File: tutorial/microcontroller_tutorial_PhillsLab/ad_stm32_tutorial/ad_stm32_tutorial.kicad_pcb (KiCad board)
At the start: 2 copper layers, 0 parts

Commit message: Started PCB Layout of power section
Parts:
- added C1: 4u7, Capacitor_SMD:C_0805_2012Metric, F.Cu at (91.8, 104.5)
- added C10: 100n, Capacitor_SMD:C_0603_1608Metric, F.Cu at (69.5, 95.4)
- added C11: 10p, Capacitor_SMD:C_0603_1608Metric, F.Cu at (69.5, 97.9)
- added C12: 10p, Capacitor_SMD:C_0603_1608Metric, F.Cu at (69.5, 100.4)
- added C13: 100n, Capacitor_SMD:C_0603_1608Metric, F.Cu at (69.5, 102.9)
- added C14: 100n, Capacitor_SMD:C_0603_1608Metric, F.Cu at (69.5, 105.4)
- added C2: 4u7, Capacitor_SMD:C_0805_2012Metric, F.Cu at (91.8, 107.5)
- added C3: 22p, Capacitor_SMD:C_0603_1608Metric, F.Cu at (65.5, 92.9)
- added C4: 100n, Capacitor_SMD:C_0603_1608Metric, F.Cu at (129.5, 95.0)
- added C5: 100n, Capacitor_SMD:C_0603_1608Metric, F.Cu at (131.5, 95.0)
- added C6: 100n, Capacitor_SMD:C_0603_1608Metric, F.Cu at (65.5, 100.4)
- added C7: 100n, Capacitor_SMD:C_0603_1608Metric, F.Cu at (65.5, 102.9)
- added C8: 100n, Capacitor_SMD:C_0603_1608Metric, F.Cu at (65.5, 105.4)
- added C9: 100n, Capacitor_SMD:C_0603_1608Metric, F.Cu at (69.5, 92.9)
- added FB1: 120R, Inductor_SMD:L_0603_1608Metric, F.Cu at (130.5, 92.5)
- added FB2: 120R, Inductor_SMD:L_6.3x6.3_H3, F.Cu at (79.8, 103.4)
- added J1: USB_C_Receptacle_USB2.0_16P, Connector_USB:USB_C_Receptacle_GCT_USB4105-xx-A_16P_TopMnt_Horizontal, F.Cu at (123.0, 91.5)
- added J2: TagConnect_TC2030-NL, Connector:Tag-Connect_TC2030-IDC-NL_2x03_P1.27mm_Vertical, F.Cu at (88.1, 94.2)
- added J3: Conn_01x06, Connector_JST:JST_EH_S6B-EH_1x06_P2.50mm_Horizontal, F.Cu at (67.2, 85.5)
- added L1: NRH2412T100MNGH, Inductor_SMD:NRH2412T2R2MNGH, F.Cu at (86.8, 105.7)
- added R1: 887k, Resistor_SMD:R_0603_1608Metric, F.Cu at (73.5, 92.9)
- added R2: 887k, Resistor_SMD:R_0603_1608Metric, F.Cu at (73.5, 95.4)
- added R3: 5k1, Resistor_SMD:R_0603_1608Metric, F.Cu at (126.2, 85.2)
- added R4: 5k1, Resistor_SMD:R_0603_1608Metric, F.Cu at (126.2, 97.8)
- added R5: 5k1, Resistor_SMD:R_0603_1608Metric, F.Cu at (73.5, 102.9)
- added U1: ~, Package_TO_SOT_SMD:SOT-23-6, F.Cu at (72.2, 109.1)
- added U2: STM32F042G6Ux, Package_DFN_QFN:QFN-28_4x4mm_P0.5mm, F.Cu at (87.2, 99.8)
- added U3: ~, Package_LGA:LGA-16_4.5x3mm_P0.5mm, F.Cu at (66.7, 109.1)
- added Y2: Crystal_GND24, Crystal:Crystal_SMD_TXC_7M-4Pin_3.2x2.5mm, F.Cu at (93.0, 98.9)
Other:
- board outline added: 35 x 25 mm

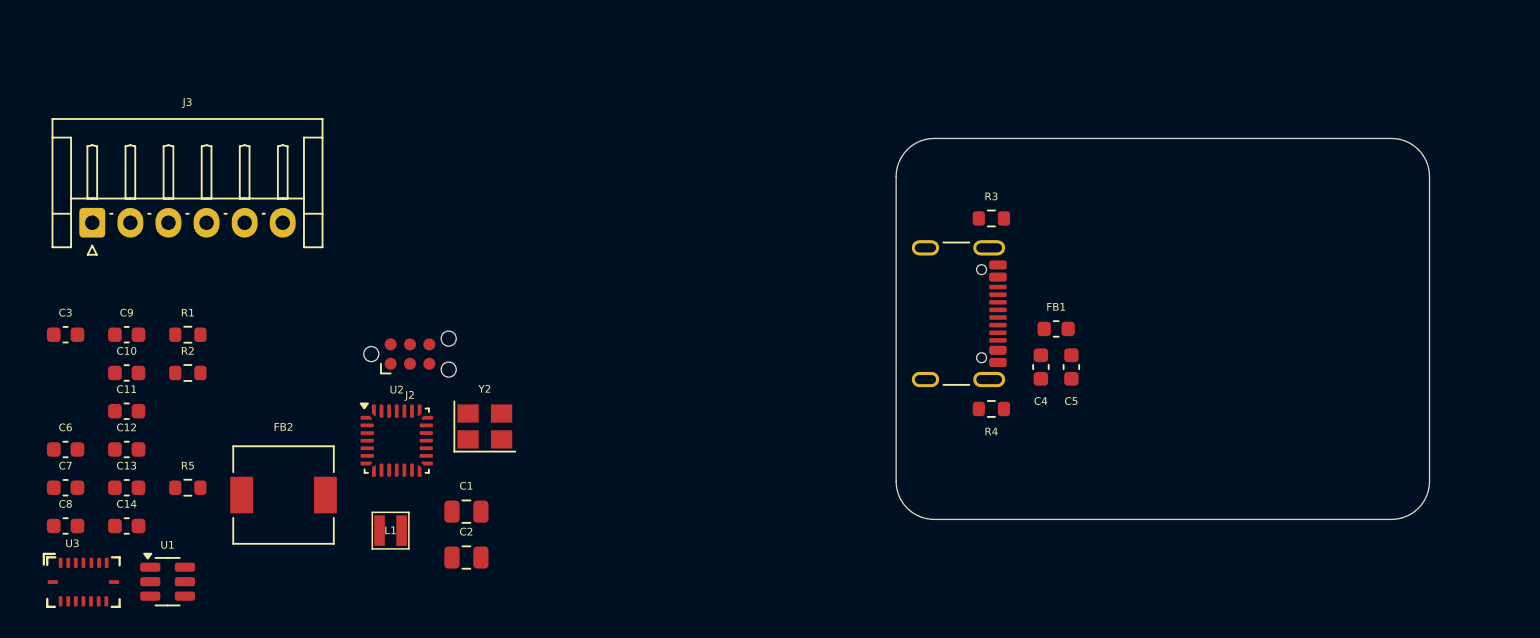
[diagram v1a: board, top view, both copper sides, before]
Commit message: Started adding MCU (STM32F4) and it's components
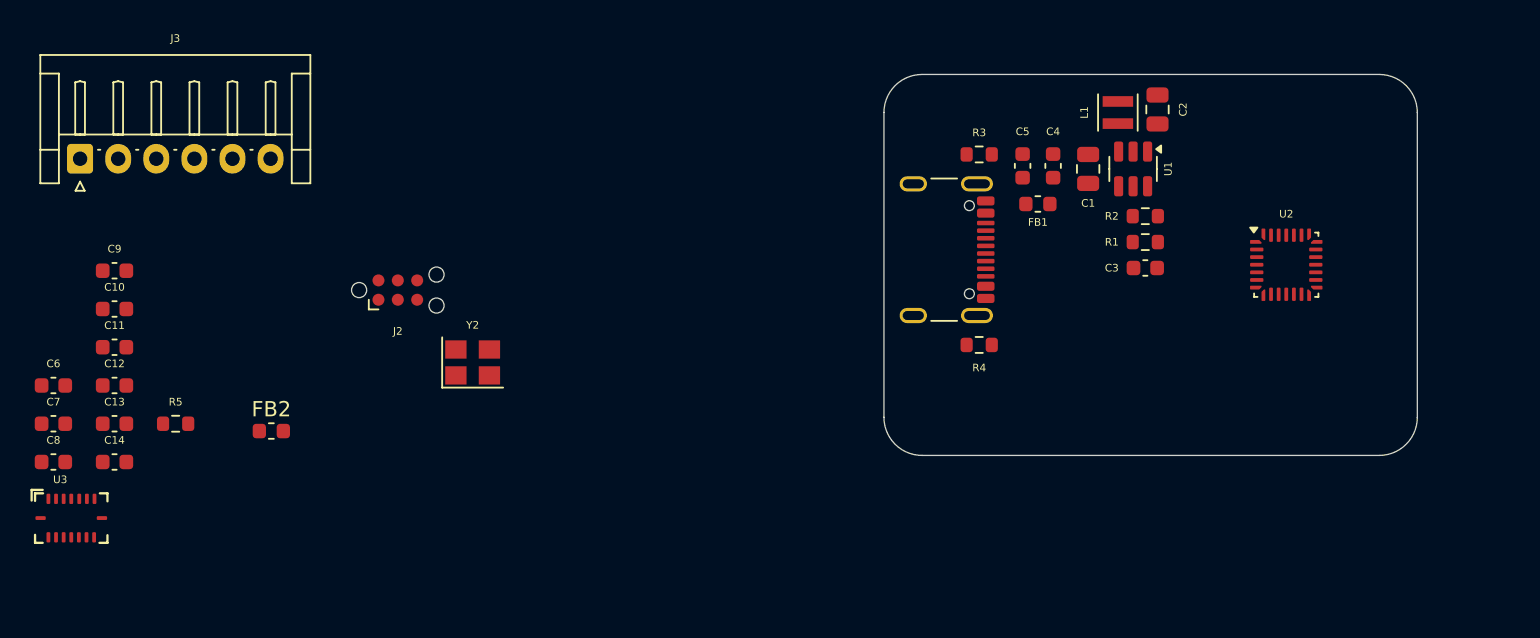
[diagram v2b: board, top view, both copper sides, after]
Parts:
- FB2: footprint Inductor_SMD:L_6.3x6.3_H3 -> Inductor_SMD:L_0603_1608Metric
- L1: footprint Inductor_SMD:NRH2412T2R2MNGH -> Inductor_SMD:L_Taiyo-Yuden_NR-24xx
- moved C3 71.0 mm to (136.3, 88.5)
- moved U1 68.9 mm to (135.6, 82.0), turned to -90 degrees
- moved R2 63.7 mm to (136.3, 85.1)
- moved R1 63.1 mm to (136.3, 86.8)
- moved U2 59.5 mm to (145.6, 88.3)
- moved L1 55.0 mm to (134.6, 78.3), turned to 90 degrees
- moved C2 54.0 mm to (137.2, 78.1), turned to -90 degrees
- moved C1 46.6 mm to (132.6, 82.0), turned to 90 degrees
- moved C5 13.6 mm to (128.3, 81.8), turned to 90 degrees
- moved C4 13.2 mm to (130.3, 81.8), turned to 90 degrees
- moved FB1 8.29 mm to (129.3, 84.3), turned to 180 degrees
- moved C10 4.28 mm to (68.7, 91.2)
- moved C11 4.28 mm to (68.7, 93.7)
- moved C12 4.28 mm to (68.7, 96.2)
- moved C13 4.28 mm to (68.7, 98.7)
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
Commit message: Finished placement of all the components
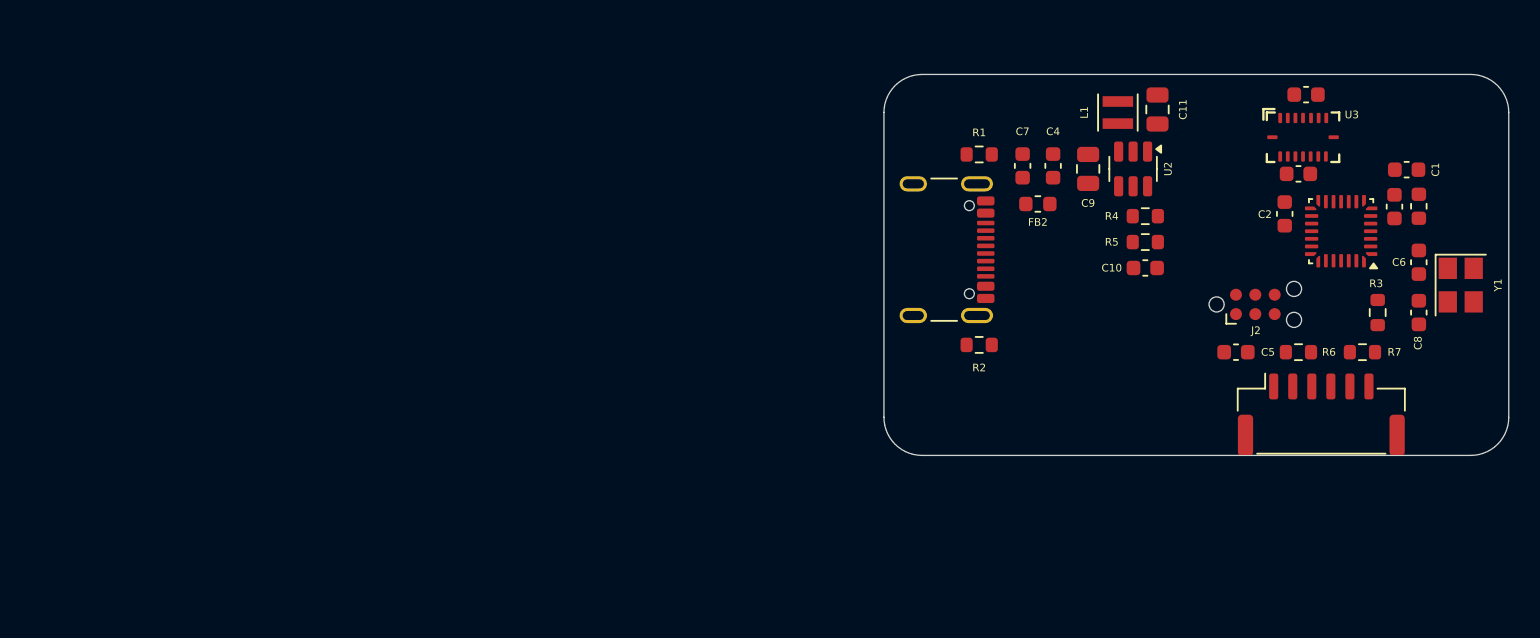
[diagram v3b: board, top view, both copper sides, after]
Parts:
- removed the C7 at (64.7, 98.7)
- added R6: 5k1, Resistor_SMD:R_0603_1608Metric, F.Cu at (146.4, 94.0)
- added R7: 5k1, Resistor_SMD:R_0603_1608Metric, F.Cu at (150.6, 94.0)
- J3: footprint Connector_JST:JST_EH_S6B-EH_1x06_P2.50mm_Horizontal -> Connector_JST:JST_GH_SM06B-GHS-TB_1x06-1MP_P1.25mm_Horizontal
- moved C1 90.8 mm to (153.5, 82.0), turned to 180 degrees
- moved C6 85.8 mm to (154.3, 88.1), turned to -90 degrees
- moved C8 85.7 mm to (154.3, 91.4), turned to 90 degrees
- moved U3 84.6 mm to (146.7, 79.9)
- moved C3 84.1 mm to (152.7, 84.5), turned to 90 degrees
- moved J3 83.2 mm to (147.9, 98.1)
- moved C12 81.8 mm to (146.9, 77.1)
- moved C2 81.6 mm to (145.5, 85.0), turned to -90 degrees
- moved C13 79.4 mm to (146.4, 82.3), turned to 180 degrees
- moved R3 79.2 mm to (151.6, 91.4), turned to -90 degrees
- moved FB1 76.7 mm to (154.3, 84.5), turned to -90 degrees
- moved C5 73.6 mm to (142.3, 94.0)
- moved Y1 65.0 mm to (157.1, 89.6), turned to -90 degrees
- moved J2 56.3 mm to (143.6, 90.9)
- moved U1 4.22 mm to (149.2, 86.1), turned to 180 degrees
- renumbered C8 to C1, C3 to C10, C2 to C11, C14 to C12, C6 to C2, C9 to C3, C10 to C5, C11 to C6, C5 to C7, C12 to C8, C1 to C9, FB2 to FB1, FB1 to FB2, R3 to R1, R4 to R2, R5 to R3, R2 to R4, R1 to R5, U2 to U1, U1 to U2, Y2 to Y1
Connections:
- U1 pad 14: unconnected-(U2-PB0-Pad14) -> IMU_INT2
- U1 pad 15: unconnected-(U2-PB1-Pad15) -> IMU_INT1
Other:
- board size 35 x 25 mm -> 41 x 25 mm

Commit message: Added mounting hole to my PCB design, it's enough for tonight. Stopped on video 9
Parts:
- added ?: , , F.Cu at (157.7, 98.1)
- added ?: , , F.Cu at (121.7, 98.3)
- added ?: , , F.Cu at (157.7, 78.3)
- added REF**: MountingHole_2.2mm_M2_DIN965_Pad, MountingHole:MountingHole_2.2mm_M2_DIN965_Pad, F.Cu at (121.7, 78.3)
- moved R1 0.25 mm to (125.7, 81.0)

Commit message: Finished power section
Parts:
- moved R1 12.5 mm to (124.4, 93.5)
- moved R2 12.5 mm to (124.4, 81.1)
- moved C10 6.03 mm to (140.7, 84.3), turned to 90 degrees
- moved R5 3.63 mm to (139.0, 84.3), turned to 90 degrees
- moved C7 1.80 mm to (130.1, 81.8)
- moved C4 1.70 mm to (128.6, 81.8)
- moved L1 0.60 mm to (133.9, 78.3)
- turned FB2 to 0 degrees
- turned R4 to 180 degrees
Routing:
- net USB_D_P: track 0.00 -> 24.6 mm
- net USB_D_N: track 0.00 -> 21.8 mm
- net VBUS: track 0.00 -> 14.5 mm, vias 0 -> 4
- net +5V: track 0.00 -> 10.3 mm
- net +3V3: track 0.00 -> 9.69 mm
- net /USB_CC1: track 0.00 -> 6.79 mm
- net /BUCK_VFB: track 0.00 -> 6.55 mm
- net GND: track 0.00 -> 2.91 mm, vias 0 -> 1
- net /BUCK_SW: track 0.00 -> 1.91 mm
- added copper zone on F.Cu, net +3V3

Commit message: Added all the traces and connecting Via's. Check out ViaStitching tool on github
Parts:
- moved C5 18.5 mm to (157.7, 83.8), turned to 90 degrees
- moved C8 3.75 mm to (154.3, 87.7), turned to -90 degrees
- moved C6 2.75 mm to (154.3, 90.9), turned to 90 degrees
- moved C13 0.23 mm to (146.2, 82.5)
- moved C12 0.20 mm to (146.9, 77.3)
- turned R6 to 0 degrees
- turned R7 to 180 degrees
- turned Y1 to 90 degrees
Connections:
- C6 pad 1: GND -> /OSC_IN
- U1 pad 2: GND -> /OSC_IN
- U1 pad 8: IMU_NCS_ACC -> IMU_NCS_GYR
- U1 pad 9: IMU_NCS_GYR -> IMU_NCS_ACC
- Y1 pad 1: GND -> /OSC_IN
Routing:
- net +3V3: track 9.69 -> 69.7 mm, vias 0 -> 6
- net /NRST: track 0.00 -> 40.0 mm
- net /OSC_IN: track 0.00 -> 12.9 mm
- net IMU_NCS_ACC: track 0.00 -> 12.1 mm
- net I2C_SCL: track 0.00 -> 12.0 mm
- net I2C_SDA: track 0.00 -> 9.79 mm
- net IMU_MISO: track 0.00 -> 8.15 mm
- net IMU_NCS_GYR: track 0.00 -> 7.97 mm
- net IMU_INT1: track 0.00 -> 7.96 mm
- net /SWDIO: track 0.00 -> 6.67 mm
- net /OSC_OUT: track 0.00 -> 6.64 mm
- net /USB_CC2: track 0.07 -> 6.20 mm
- net GND: track 2.91 -> 8.54 mm, vias 1 -> 100
- net /SWCLK: track 0.00 -> 5.35 mm
- net IMU_SCK: track 0.00 -> 5.13 mm
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
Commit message: Checking DRC
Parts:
- removed ? (x3): , 
- added REF**: MountingHole_2.2mm_M2_DIN965_Pad, MountingHole:MountingHole_2.2mm_M2_DIN965_Pad, F.Cu at (157.2, 78.8)
- added REF**: MountingHole_2.2mm_M2_DIN965_Pad, MountingHole:MountingHole_2.2mm_M2_DIN965_Pad, F.Cu at (122.2, 97.8)
- added REF**: MountingHole_2.2mm_M2_DIN965_Pad, MountingHole:MountingHole_2.2mm_M2_DIN965_Pad, F.Cu at (157.2, 97.8)
- moved REF** 0.35 mm to (122.0, 78.5)
- moved R2 0.14 mm to (124.5, 81.1)
- moved R1 0.12 mm to (124.5, 93.5)
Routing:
- added copper zone on B.Cu, net GND
- added copper zone on F.Cu, net GND

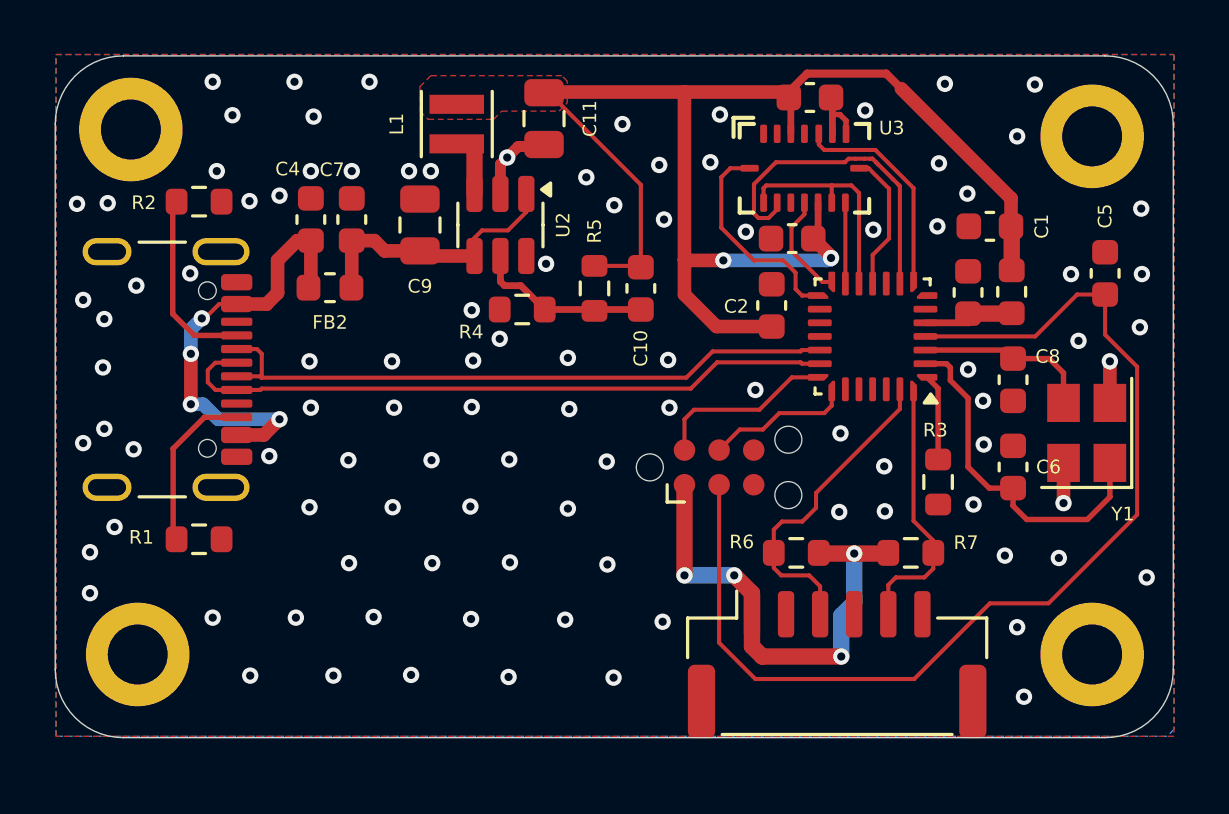
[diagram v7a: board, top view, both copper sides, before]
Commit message: Finished PCB design, just need to add silkscreen
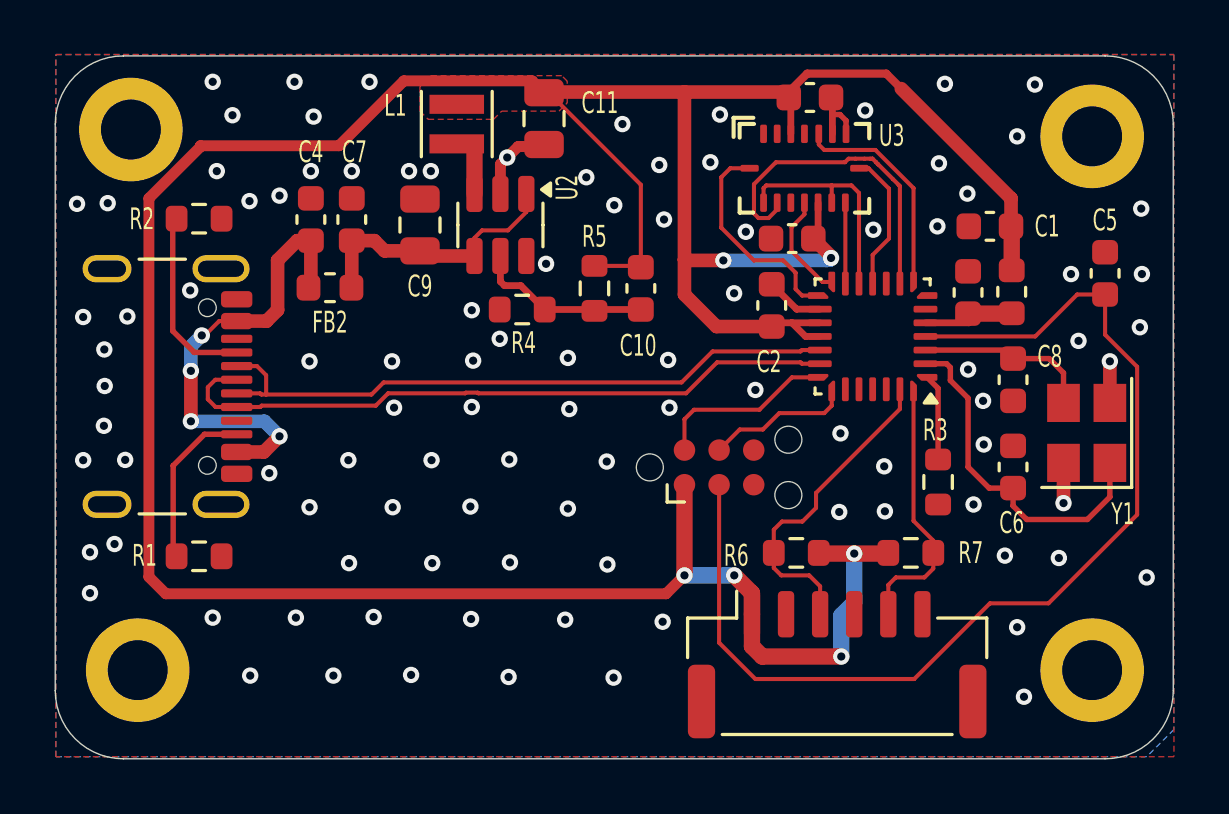
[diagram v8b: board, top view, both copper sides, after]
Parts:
- moved J1 0.62 mm to (122.2, 87.9)
- moved R1 0.62 mm to (124.5, 94.2)
- moved R2 0.62 mm to (124.5, 81.8)
- moved REF** 0.58 mm to (122.2, 98.3)
- moved REF** 0.58 mm to (157.2, 98.3)
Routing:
- net +3V3: track 69.9 -> 123.4 mm
- net GND: track 8.54 -> 10.7 mm
- net VBUS: track 16.3 -> 16.9 mm
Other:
- board size 41 x 25 mm -> 41 x 25.8 mm
